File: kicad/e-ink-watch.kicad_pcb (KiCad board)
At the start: 4 copper layers, 40 x 40 mm, 42 parts, among them SW1 BTN1, SW2 BTN2, SW3 BTN3, U1 MDBT50Q-1MV2, U2 BQ25120A

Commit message: Reconnect U2 CD E2 and ILIM C2 with orthogonal dogbones.
CD uses a south-of-E2 via and B.Cu L at x=112.65, not via-in-pad
or a B.Cu run at x=112.4 that clips the 3V3 via. ILIM L-jogs to
the existing via instead of dropping onto the VBAT street.

Co-authored-by: illiapliukhin <illiapliukhin@users.noreply.github.com>
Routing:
- net CD: track 2.08 -> 6.39 mm, vias 1 -> 2
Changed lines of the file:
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@@
+	)
+	(via
+		(at 110.6 106.95)
+		(size 0.25)
+		(drill 0.15)
+		(layers "F.Cu" "B.Cu")
+		(net 32)
+	)
+	(segment
+		(start 110.6 106.8)
+		(end 110.6 106.95)
+		(width 0.15)
+		(layer "F.Cu")
+		(net 32)
+	)
+	(segment
+		(start 110.6 106.95)
+		(end 112.65 106.95)
+		(width 0.12)
+		(layer "B.Cu")
+		(net 32)
+	)
+	(segment
+		(start 112.65 106.95)
+		(end 112.65 108.41)
+		(width 0.12)
+		(layer "B.Cu")
+		(net 32)
+	)
+	(segment
+		(start 112.65 108.41)
+		(end 113.3 108.41)
+		(width 0.12)
+		(layer "B.Cu")
+		(net 32)
+	)
+	(segment
+		(start 110.6 106.0)
+		(end 110.75 106.0)
+		(width 0.08)
+		(layer "F.Cu")
+		(net 35)
+	)
+	(segment
+		(start 110.75 106.0)
+		(end 110.75 105.8)
+		(width 0.08)
+		(layer "F.Cu")
+		(net 35)
 	)
 	(via

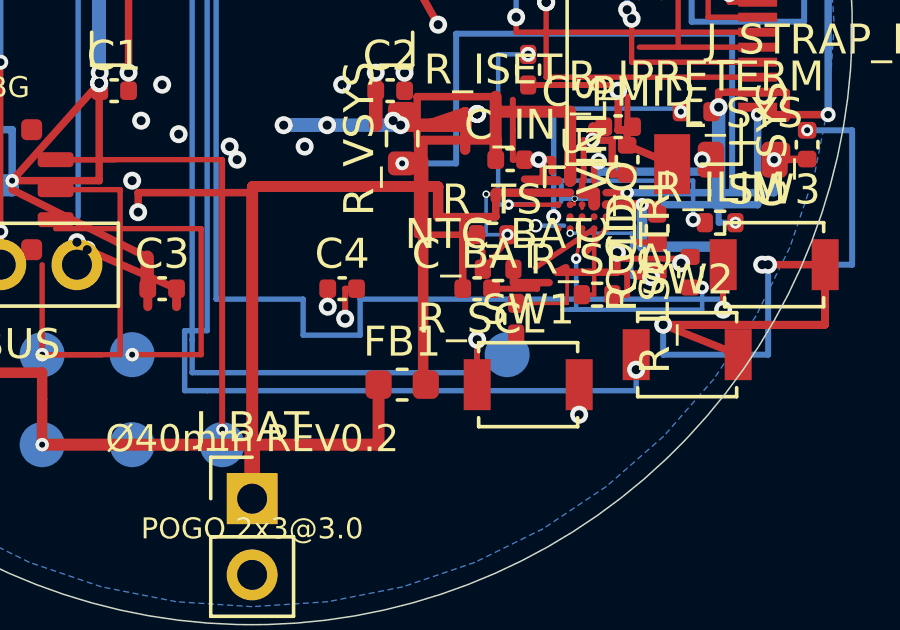
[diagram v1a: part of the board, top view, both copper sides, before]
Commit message: Spread R_SCL west off the south 0402 heap.
Sol wanted R_SDA on SW1/SW2 courtyards; keep the pull-up in the SDA
street and move R_SCL to (106.5, 110.1, 90) with the 3V3 L retargeted.
DRC shorting=0, unc=12.

Co-authored-by: illiapliukhin <illiapliukhin@users.noreply.github.com>
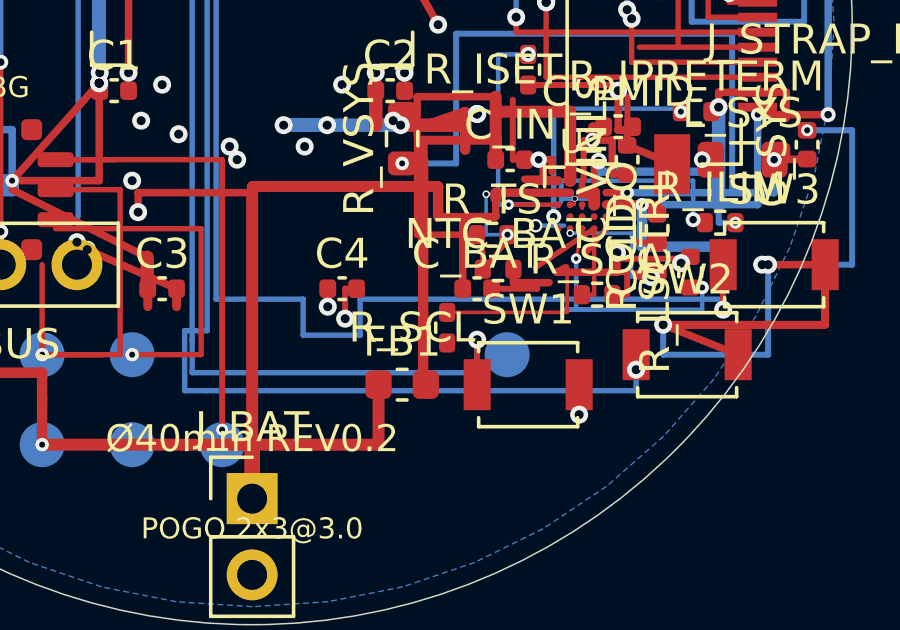
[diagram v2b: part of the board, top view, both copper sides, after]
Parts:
- moved R_SCL 2.32 mm to (106.5, 110.1)
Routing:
- net 3V3: track 103.1 -> 105.7 mm
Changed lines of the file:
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@@
 	(footprint "Resistor_SMD:R_0402_1005Metric"
 		(layer "F.Cu")
-		(at 108.8 109.8 90)
+		(at 106.5 110.1 90)
 		(descr "Resistor SMD 0402 (1005 Metric), square (rectangular) end terminal, IPC-7351 nominal, (Body size source: IPC-SM-782 page 72, https://www.pcb-3d.com/wordpress/wp-content/uploads/ipc-sm-782a_amendment_1_and_2.pdf), generated with kicad-footprint-generator")
 		(tags "resistor")
@@
 	)
 	(segment
-		(start 108.8 109.29)
-		(end 110.5 109.29)
+		(start 106.5 109.59)
+		(end 110.5 109.59)
 		(width 0.12)
 		(layer "F.Cu")
@@
 	)
 	(segment
-		(start 110.5 109.29)
+		(start 110.5 109.59)
 		(end 110.5 108.25)
 		(width 0.12)

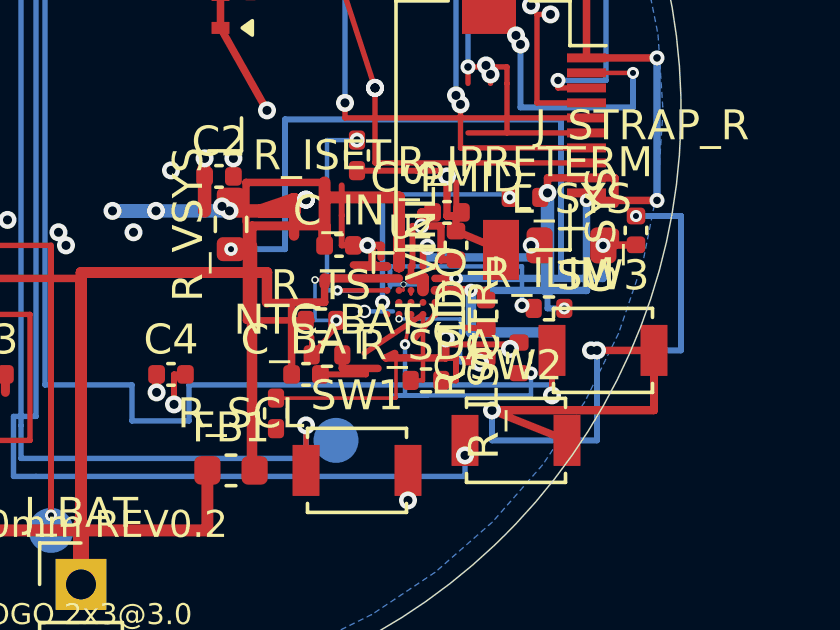
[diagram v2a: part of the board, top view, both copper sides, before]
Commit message: Tie U2 D5 GND onto east R_CD without zone refill.
Sol STEP5 refused SCL/TS (pad1 boxed by VBUS/BTN1; TS B hits CD/ILIM).
Independent KEEP: D5 via 0.25@(112.4,106.55) plus F.Cu L onto existing
R_CD GND (112.8,107.24). DRC shorting=0, unconnected 12→10.

Co-authored-by: illiapliukhin <illiapliukhin@users.noreply.github.com>
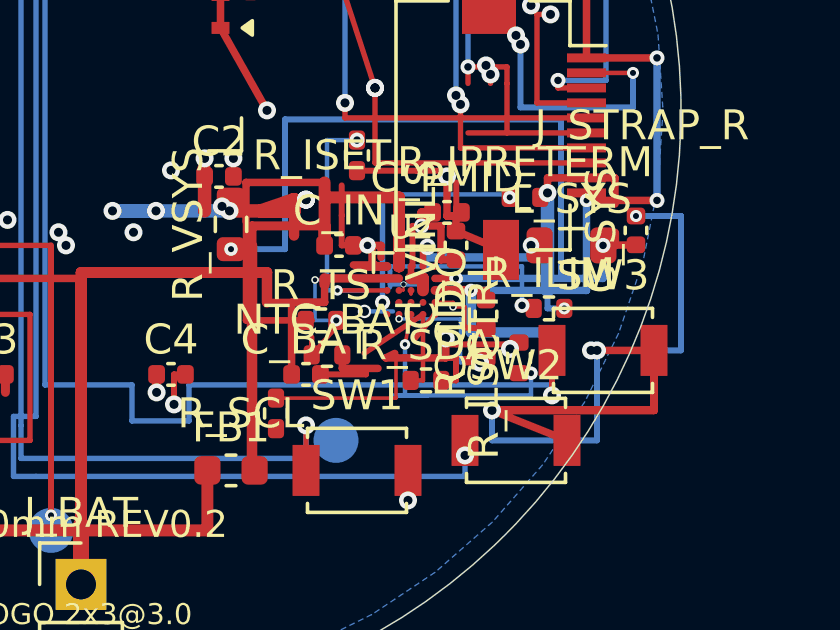
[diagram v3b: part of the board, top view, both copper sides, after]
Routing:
- net GND: track 139.0 -> 140.9 mm, vias 43 -> 44
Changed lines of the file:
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@@
+	)
+	(via
+		(at 112.4 106.55)
+		(size 0.25)
+		(drill 0.15)
+		(layers "F.Cu" "B.Cu")
+		(net 1)
+	)
+	(segment
+		(start 111.8 106.4)
+		(end 112.4 106.4)
+		(width 0.12)
+		(layer "F.Cu")
+		(net 1)
+	)
+	(segment
+		(start 112.4 106.4)
+		(end 112.4 106.55)
+		(width 0.12)
+		(layer "F.Cu")
+		(net 1)
+	)
+	(segment
+		(start 112.4 106.55)
+		(end 112.8 106.55)
+		(width 0.12)
+		(layer "F.Cu")
+		(net 1)
+	)
+	(segment
+		(start 112.8 106.55)
+		(end 112.8 107.24)
+		(width 0.12)
+		(layer "F.Cu")
+		(net 1)
 	)
 	(via

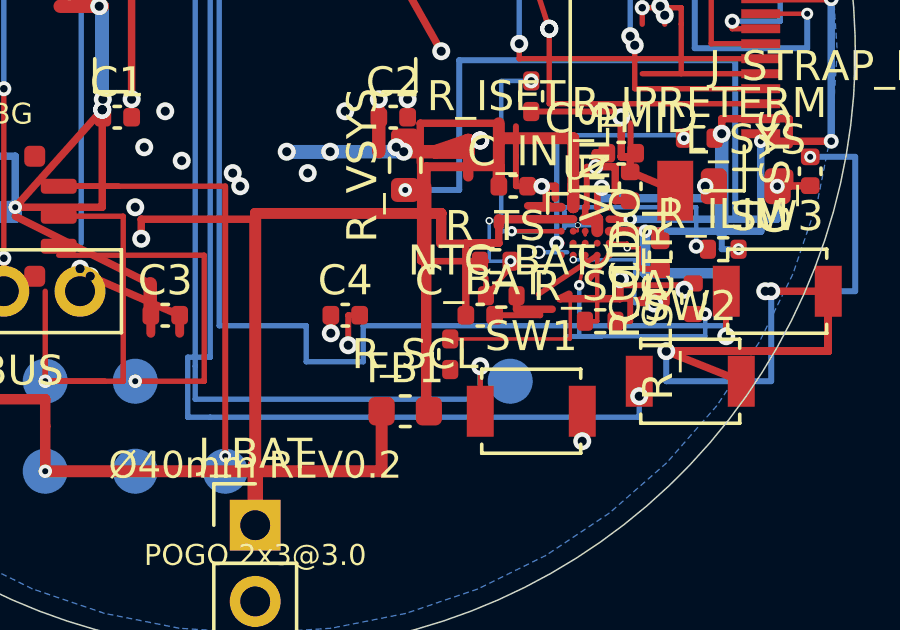
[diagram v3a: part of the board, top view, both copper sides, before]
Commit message: Stitch east 3V3 to the west via north of BTN3.
Sol STEP6 refused the F.Cu haul across VBUS. Independent KEEP: via on
the existing 3V3 F rail at (110.4,108.25) plus B.Cu L at y=108.55 onto
west via (102.52,109.40) through the BTN3 U north opening.
DRC shorting=0, unconnected 10→9.

Co-authored-by: illiapliukhin <illiapliukhin@users.noreply.github.com>
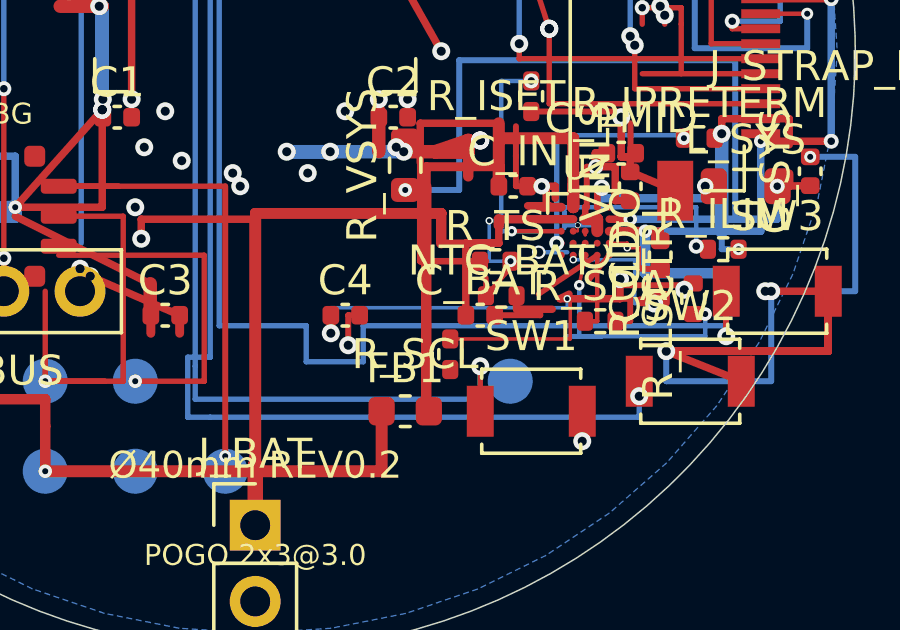
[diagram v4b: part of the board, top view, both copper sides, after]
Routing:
- net 3V3: track 105.7 -> 114.8 mm, vias 25 -> 26
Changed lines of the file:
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@@
+	)
+	(via
+		(at 110.4 108.25)
+		(size 0.25)
+		(drill 0.15)
+		(layers "F.Cu" "B.Cu")
+		(net 2)
+	)
+	(segment
+		(start 110.4 108.25)
+		(end 110.4 108.55)
+		(width 0.12)
+		(layer "B.Cu")
+		(net 2)
+	)
+	(segment
+		(start 110.4 108.55)
+		(end 102.52 108.55)
+		(width 0.12)
+		(layer "B.Cu")
+		(net 2)
+	)
+	(segment
+		(start 102.52 108.55)
+		(end 102.52 109.4)
+		(width 0.12)
+		(layer "B.Cu")
+		(net 2)
 	)
 	(via

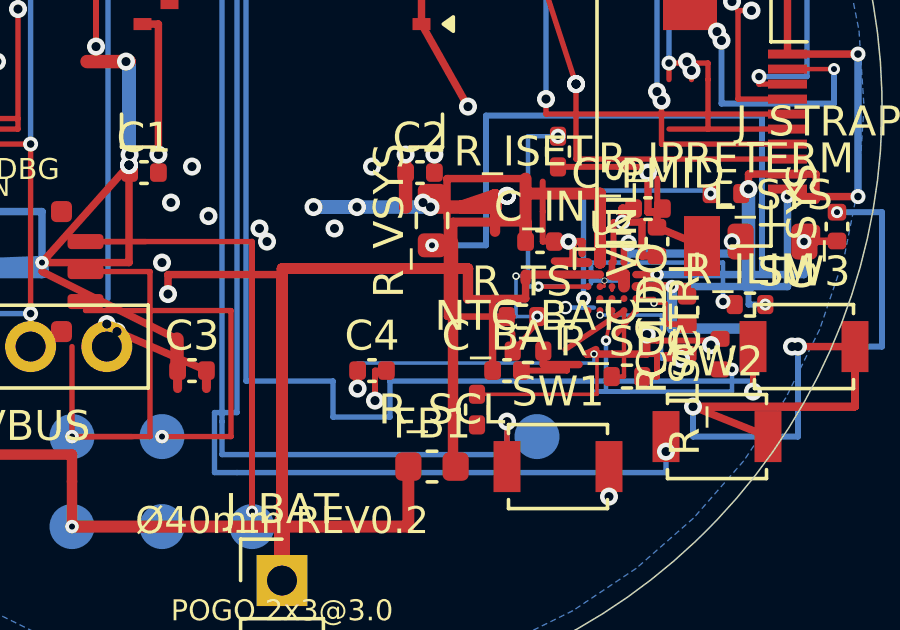
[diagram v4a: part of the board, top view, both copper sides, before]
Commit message: Spread NTC_BAT west onto the C4 column.
Park the 0402 NTC on the C4 column west of VBUS so the south U2 heap is not stacked on C_BAT. TS hops B.Cu under VBUS at y=107.55 onto the existing TS via; GND ties F.Cu onto C4.2. Sol STEP7 independently refused the east/south NTC and north R_SDA paths.

Co-authored-by: illiapliukhin <illiapliukhin@users.noreply.github.com>
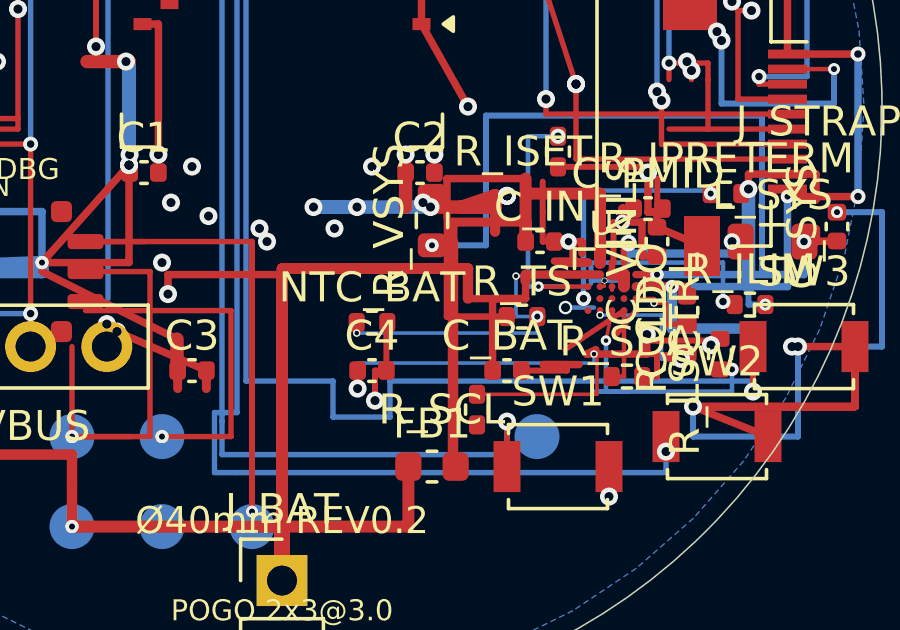
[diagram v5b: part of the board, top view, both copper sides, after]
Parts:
- moved NTC_BAT 5.29 mm to (103.0, 107.2)
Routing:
- net TS: track 7.16 -> 12.3 mm, vias 2 -> 3
- net GND: track 140.9 -> 142.9 mm
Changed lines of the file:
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@@
 	(footprint "R_0402_1005Metric"
 		(layer "F.Cu")
-		(at 108.2 108.15)
+		(at 103.0 107.2)
 		(descr "Resistor SMD 0402 (1005 Metric), square (rectangular) end terminal, IPC-7351 nominal, (Body size source: IPC-SM-782 page 72, https://www.pcb-3d.com/wordpress/wp-content/uploads/ipc-sm-782a_amendment_1_and_2.pdf), generated with kicad-footprint-generator")
 		(tags "resistor")
@@
 	)
 	(segment
-		(start 108.71 108.15)
-		(end 108.71 108.6)
+		(start 108.71 108.6)
+		(end 109.5 108.6)
 		(width 0.25)
 		(layer "F.Cu")
@@
 	)
 	(segment
-		(start 108.71 107.0)
-		(end 107.69 108.15)
+		(start 108.51 107.0)
+		(end 108.71 107.0)
 		(width 0.15)
 		(layer "F.Cu")
@@
 	)
 	(via
+		(at 102.49 107.55)
+		(size 0.25)
+		(drill 0.15)
+		(layers "F.Cu" "B.Cu")
+		(net 31)
+	)
+	(segment
+		(start 102.49 107.2)
+		(end 102.49 107.55)
+		(width 0.15)
+		(layer "F.Cu")
+		(net 31)
+	)
+	(segment
+		(start 102.49 107.55)
+		(end 108.51 107.55)
+		(width 0.12)
+		(layer "B.Cu")
+		(net 31)
+	)
+	(segment
+		(start 108.51 107.55)
+		(end 108.51 107.0)
+		(width 0.12)
+		(layer "B.Cu")
+		(net 31)
+	)
+	(segment
+		(start 103.51 107.2)
+		(end 103.48 107.2)
+		(width 0.2)
+		(layer "F.Cu")
+		(net 1)
+	)
+	(segment
+		(start 103.48 107.2)
+		(end 103.48 108.8)
+		(width 0.2)
+		(layer "F.Cu")
+		(net 1)
+	)
+	(via
 		(at 111.35 103.85)
 		(size 0.5)
@@
 	)
 	(segment
-		(start 107.69 108.15)
-		(end 107.69 107.55)
+		(start 108.51 107.0)
+		(end 108.51 107.12)
 		(width 0.18)
 		(layer "F.Cu")

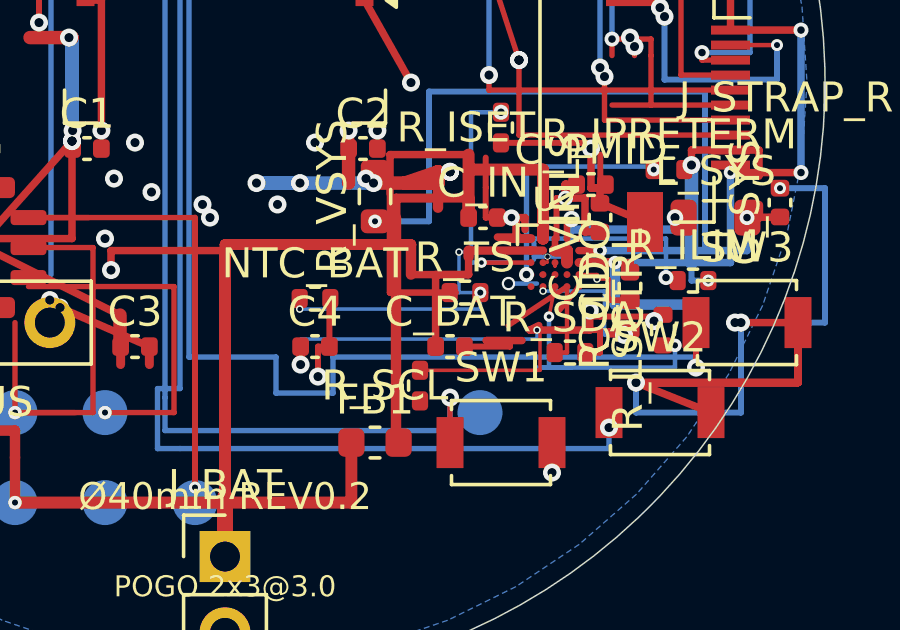
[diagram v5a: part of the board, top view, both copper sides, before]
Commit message: Spread C_BAT north off the R_SCL courtyard.
Slide C_BAT to (107.5, 108.5) so the remaining 0402–0402 courtyard pile is gone. VBAT and GND follows stay orthogonal. Sol STEP8 probed R_SDA off SW2 (north, rot90, rot180) and every path still overlaps 3V3 x=110.5 or SDA x=111.4; no R_SDA copper applied.

Co-authored-by: illiapliukhin <illiapliukhin@users.noreply.github.com>
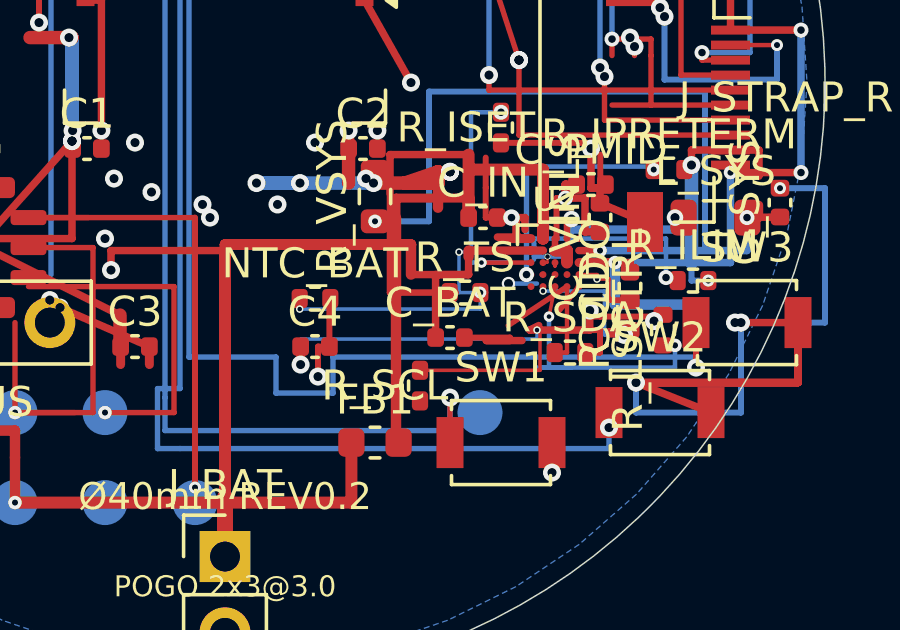
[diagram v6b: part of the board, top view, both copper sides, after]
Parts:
- moved C_BAT 0.30 mm to (107.5, 108.5)
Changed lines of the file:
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@@
 	(footprint "Capacitor_SMD:C_0402_1005Metric"
 		(layer "F.Cu")
-		(at 107.5 108.8)
+		(at 107.5 108.5)
 		(descr "Capacitor SMD 0402 (1005 Metric), square (rectangular) end terminal, IPC-7351 nominal, (Body size source: IPC-SM-782 page 76, https://www.pcb-3d.com/wordpress/wp-content/uploads/ipc-sm-782a_amendment_1_and_2.pdf), generated with kicad-footprint-generator")
 		(tags "capacitor")
@@
 	)
 	(segment
-		(start 107.02 108.8)
+		(start 107.02 108.5)
 		(end 107.02 106.4)
 		(width 0.25)
@@
 	)
 	(segment
-		(start 107.98 108.8)
-		(end 109.5 108.8)
+		(start 107.98 108.5)
+		(end 109.5 108.5)
 		(width 0.2)
 		(layer "F.Cu")
@@
 	)
 	(segment
-		(start 109.5 108.8)
+		(start 109.5 108.5)
 		(end 109.5 108.6)
 		(width 0.2)

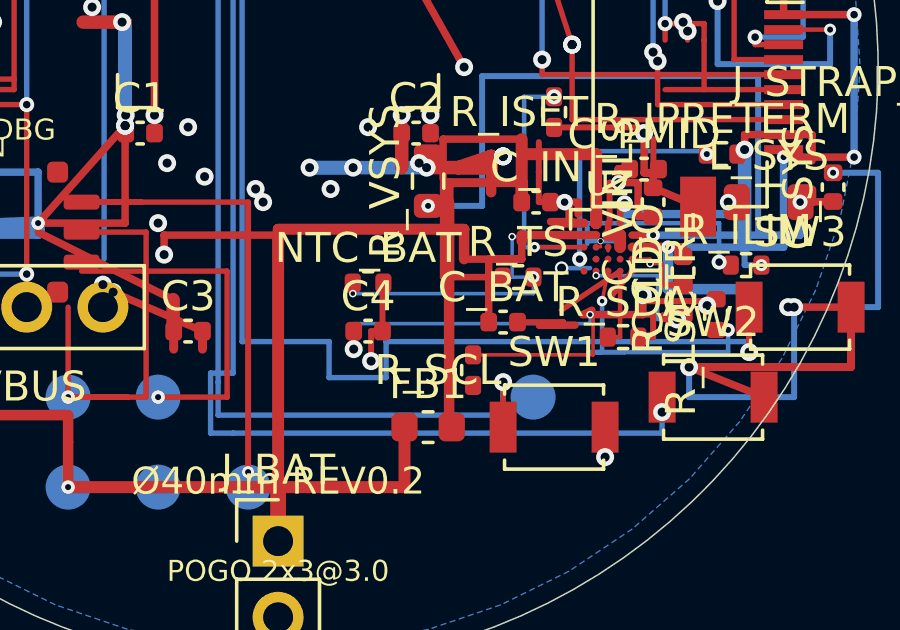
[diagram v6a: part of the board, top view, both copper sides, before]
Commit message: Join C_BAT GND to the C4 column under VBUS.
Stitch C_BAT pad2 to the west GND column with 0.25 vias at (103.48, 108.05) and (107.98, 108.05) plus B.Cu at y=108.05 between the TS and 3V3 back-side rails. Unconnected 9→8, shorting stays 0. Explorer now finalizes after the last tool round so Sol KEEP text is not dropped.

Co-authored-by: illiapliukhin <illiapliukhin@users.noreply.github.com>
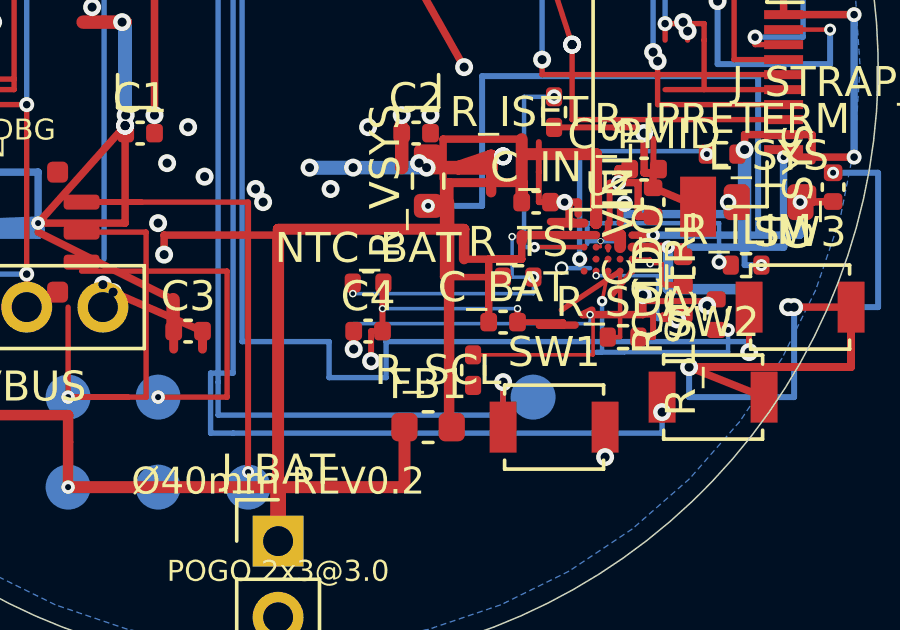
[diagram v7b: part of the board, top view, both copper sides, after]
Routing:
- net GND: track 142.8 -> 147.7 mm, vias 44 -> 46
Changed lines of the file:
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@@
+	)
+	(via
+		(at 103.48 108.05)
+		(size 0.25)
+		(drill 0.15)
+		(layers "F.Cu" "B.Cu")
+		(net 1)
+	)
+	(via
+		(at 107.98 108.05)
+		(size 0.25)
+		(drill 0.15)
+		(layers "F.Cu" "B.Cu")
+		(net 1)
+	)
+	(segment
+		(start 103.48 108.05)
+		(end 107.98 108.05)
+		(width 0.12)
+		(layer "B.Cu")
+		(net 1)
+	)
+	(segment
+		(start 107.98 108.5)
+		(end 107.98 108.05)
+		(width 0.2)
+		(layer "F.Cu")
+		(net 1)
 	)
 	(via
